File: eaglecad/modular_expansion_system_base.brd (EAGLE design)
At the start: 90.2 x 100 mm, 36 parts, among them IC1 74LS244N, IC2 74LS244N, IC3 74LS244N, IC4 SRAM, IC5 74LS30N, IC6 74LS30N, IC7 7805T, IC8 74LS00N, IC9 7805T, J1_ADDRESS_CON j1, J2_DATA_AND_POWER_CON j2, J3 interrupt_wait_block, SW1 100SP3T1B1M6QE

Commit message: all three boards designed
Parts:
- removed C9: .1uf, rcl:C025-025X050
- removed IC5: 74LS30N, 74xx-us:DIL14
- removed J3: interrupt_wait_block, SparkFun-Connectors:1X20
- removed RN1: 4.7k, resistor-dil:DIL16
- added J1-WAIT-AND-INT: WAIT-AND-INT, SparkFun-Connectors:2X4
- IC6: value 74LS30N -> 74LS20N
- RN2: device resistor-dil:DIL16 -> resistor-sil:SIL9
- moved C6 38.3 mm to (58.4, 77.5)
- moved RN2 17.2 mm to (80.6, 75.6), turned to 90 degrees
- moved IC6 7.96 mm to (69.2, 77.5), turned to 0 degrees
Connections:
- removed net INT*0: IC5.12, J3.1, RN2.8
- removed net INT*1: IC5.11, J3.2, RN2.7
- removed net INT*2: IC5.6, J3.3, RN2.6
- removed net INT*3: IC5.5, J3.4, RN2.5
- removed net INT*4: IC5.4, J3.5, RN2.4
- removed net INT*5: IC5.3, J3.6, RN2.3
- removed net INT*6: IC5.2, J3.7, RN2.2
- removed net INT*7: IC5.1, J3.8, RN2.1
- removed net N$21: IC6.3, J3.18, RN1.3
- removed net WAIT*0: IC6.12, J3.13, RN1.8
- removed net WAIT*1: IC6.11, J3.14, RN1.7
- removed net WAIT*2: IC6.6, J3.15, RN1.6
- removed net WAIT*3: IC6.5, J3.16, RN1.5
- removed net WAIT*5: IC6.4, J3.17, RN1.4
- removed net WAIT*6: IC6.2, J3.19, RN1.2
- removed net WAIT*7: IC6.1, J3.20, RN1.1
- new net INT0*: IC6.5, J1-WAIT-AND-INT.1, RN2.2
- new net INT1*: IC6.4, J1-WAIT-AND-INT.3, RN2.3
- new net INT2*: IC6.2, J1-WAIT-AND-INT.5, RN2.4
- new net INT3*: IC6.1, J1-WAIT-AND-INT.7, RN2.5
- new net WAIT0*: IC6.13, J1-WAIT-AND-INT.2, RN2.6
- new net WAIT1*: IC6.12, J1-WAIT-AND-INT.4, RN2.7
- new net WAIT2*: IC6.10, J1-WAIT-AND-INT.6, RN2.8
- new net WAIT3*: IC6.9, J1-WAIT-AND-INT.8, RN2.9
- net GND: no longer C9.2, IC5.7
- net INT: now also IC6.6; no longer IC5.8
- net VCC: now also RN2.1; no longer C9.1, IC5.14, RN1.10, RN1.11, RN1.12, RN1.13, RN1.14, RN1.15, RN1.16, RN1.9, RN2.10, RN2.11, RN2.12, RN2.13, RN2.14, RN2.15, RN2.16, RN2.9
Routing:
- net WAIT*0: track 67.5 -> 0.00 mm
- net INT2*: track 0.00 -> 58.1 mm
- net INT3*: track 0.00 -> 51.6 mm
- net WAIT*1: track 48.9 -> 0.00 mm, vias 2 -> 0
- net INT*0: track 42.1 -> 0.00 mm, vias 1 -> 0
- net INT*2: track 40.8 -> 0.00 mm
- net INT*3: track 39.5 -> 0.00 mm
- net WAIT*2: track 39.4 -> 0.00 mm
- net INT*7: track 39.0 -> 0.00 mm
- net WAIT*6: track 38.6 -> 0.00 mm
- net N$21: track 37.3 -> 0.00 mm
- net INT*4: track 36.7 -> 0.00 mm
- net WAIT*7: track 36.4 -> 0.00 mm
- net WAIT*5: track 36.3 -> 0.00 mm
- net WAIT*3: track 35.3 -> 0.00 mm
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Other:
- board text added: "INT*"
- board text added: "WAIT*"
- board text removed: "IN*0"
- board text removed: "IN*1"
- board text removed: "IN*2"
- board text removed: "IN*3"
- board text removed: "IN*4"
- board text removed: "IN*5"
- board text removed: "IN*6"
- board text removed: "IN*7"
- board text removed: "W0*"
- board text removed: "W1*"
- board text removed: "W2*"
- board text removed: "W3*"
- board text removed: "W4*"
- board text removed: "W5*"
- board text removed: "W6*"
- board text removed: "W7*"

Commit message: added text to boards
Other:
- board text added: "TRS80MXS Base - V1.0 Joe Rounceville (C) 2019"
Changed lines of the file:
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@@
 <text x="63.5" y="92.3925" size="1.778" layer="25" rot="R270">WAIT*</text>
 <text x="74.295" y="86.36" size="1.778" layer="25" rot="R90">INT*</text>
+<text x="82.55" y="31.75" size="1.778" layer="25" rot="R90">TRS80MXS Base - V1.0
+Joe Rounceville (C) 2019</text>
 </plain>
 <attributes>
@@
 </drawing>
 <compatibility>
+<note version="6.3" minversion="6.2.2" severity="warning">
+Since Version 6.2.2 text objects can contain more than one line,
+which will not be processed correctly with this version.
+</note>
 <note version="8.2" severity="warning">
 Since Version 8.2, EAGLE supports online libraries. The ids

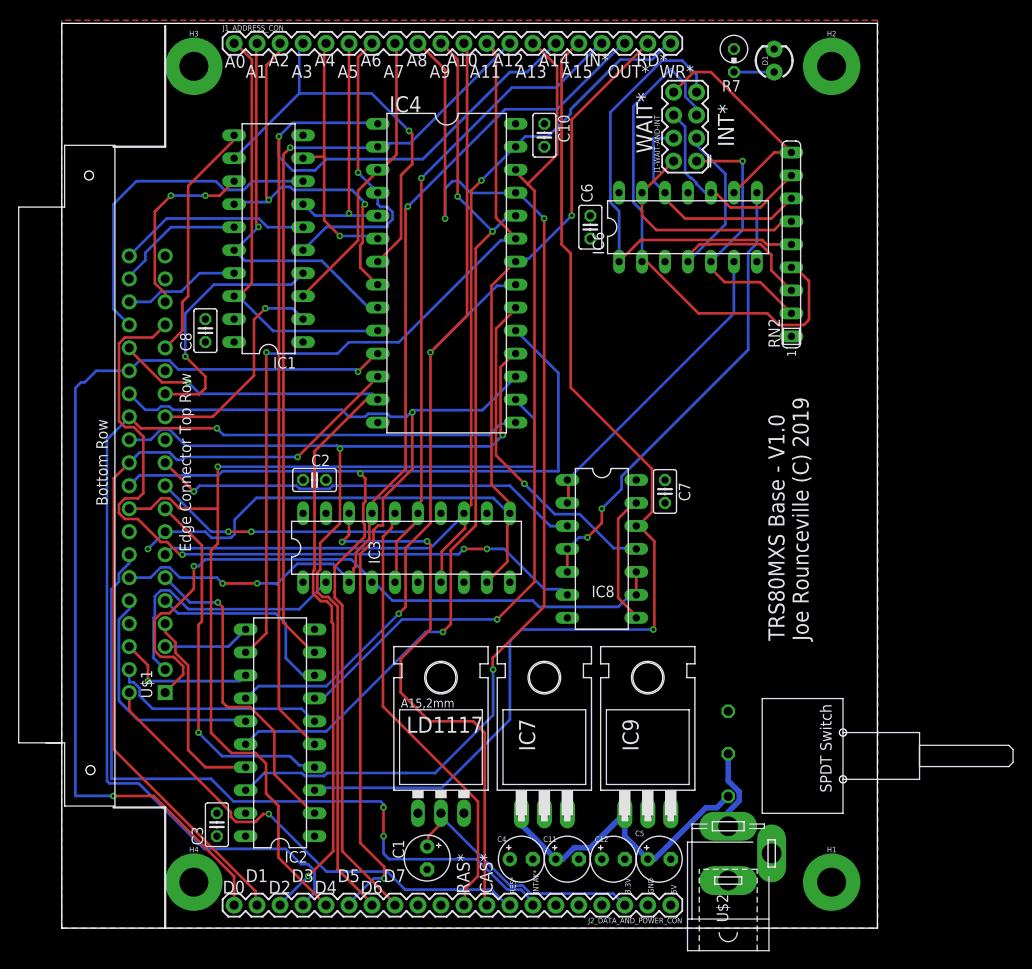
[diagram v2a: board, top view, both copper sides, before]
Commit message: removed soft reset for vdp, added 12 voice sound
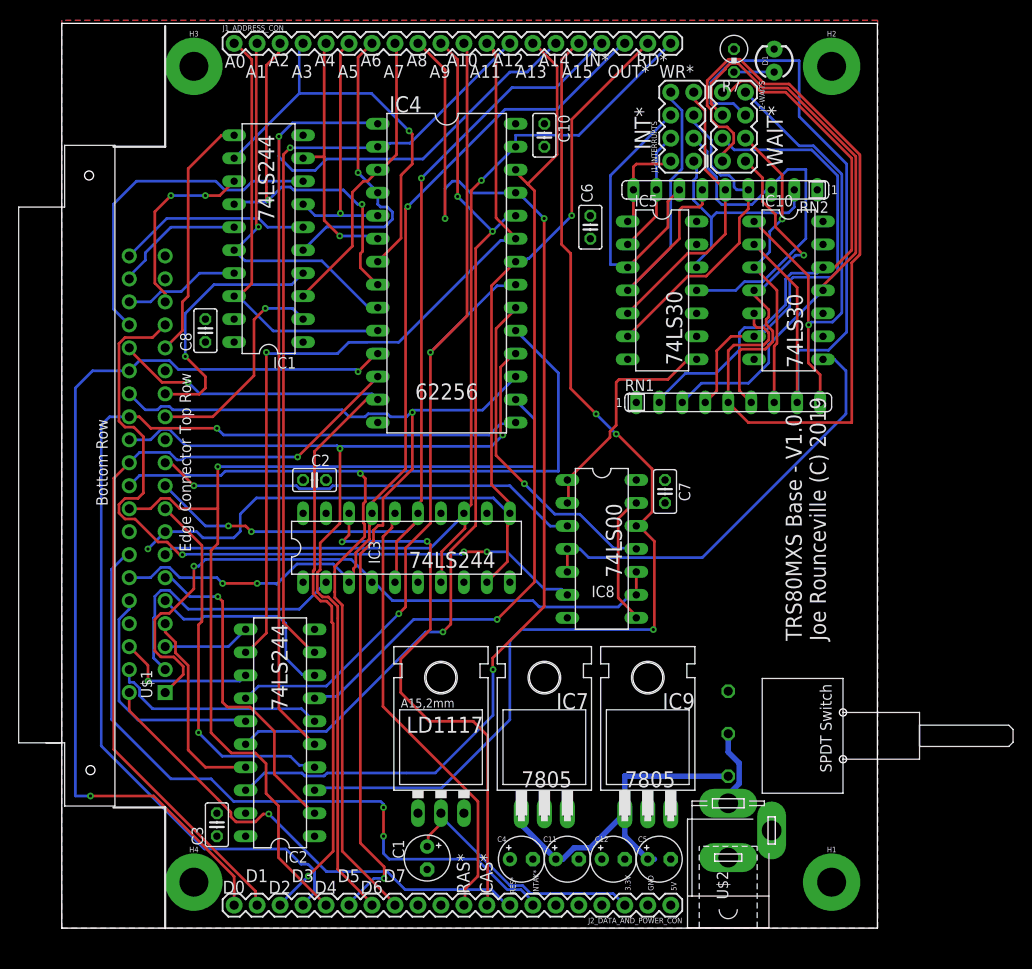
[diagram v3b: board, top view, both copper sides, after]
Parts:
- removed IC6: 74LS20N, 74xx-us:DIL14
- removed J1-WAIT-AND-INT: WAIT-AND-INT, SparkFun-Connectors:2X4
- added IC10, IC5: 74LS30N, 74xx-us:DIL14
- added J1-INTERRUPTS: INTERRUPTS, SparkFun-Connectors:2X4
- added J2-WAITS: WAITS, SparkFun-Connectors:2X4
- added RN1: 4.7k, resistor-sil:SIL9
- moved RN2 9.47 mm to (73.3, 81.6), turned to 180 degrees
- moved U$2 2.54 mm to (73.7, 10.8)
- moved SW1 2.22 mm to (73.7, 25.7)
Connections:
- new net INT4*: IC5.1, J1-INTERRUPTS.2, RN2.9
- new net INT5*: IC5.2, J1-INTERRUPTS.4, RN2.8
- new net INT6*: IC5.3, J1-INTERRUPTS.6, RN2.7
- new net INT7*: IC5.4, J1-INTERRUPTS.8, RN2.6
- new net WAIT4*: IC10.5, J2-WAITS.7, RN1.5
- new net WAIT5*: IC10.6, J2-WAITS.5, RN1.4
- new net WAIT6*: IC10.11, J2-WAITS.3, RN1.3
- new net WAIT7*: IC10.12, J2-WAITS.1, RN1.2
- net GND: now also IC10.7, IC5.7; no longer IC6.7
- net INT: now also IC5.8; no longer IC6.6
- net INT0*: now also IC5.12, J1-INTERRUPTS.1; no longer IC6.5, J1-WAIT-AND-INT.1
- net INT1*: now also IC5.11, J1-INTERRUPTS.3; no longer IC6.4, J1-WAIT-AND-INT.3
- net INT2*: now also IC5.6, J1-INTERRUPTS.5; no longer IC6.2, J1-WAIT-AND-INT.5
- net INT3*: now also IC5.5, J1-INTERRUPTS.7; no longer IC6.1, J1-WAIT-AND-INT.7
- net VCC: now also IC10.14, IC5.14, RN1.1; no longer IC6.14
- net WAIT: now also IC10.8; no longer IC6.8
- net WAIT0*: now also IC10.4, J2-WAITS.8, RN1.6; no longer IC6.13, J1-WAIT-AND-INT.2, RN2.6
- net WAIT1*: now also IC10.3, J2-WAITS.6, RN1.7; no longer IC6.12, J1-WAIT-AND-INT.4, RN2.7
- net WAIT2*: now also IC10.2, J2-WAITS.4, RN1.8; no longer IC6.10, J1-WAIT-AND-INT.6, RN2.8
- net WAIT3*: now also IC10.1, J2-WAITS.2, RN1.9; no longer IC6.9, J1-WAIT-AND-INT.8, RN2.9
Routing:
- net WAIT4*: track 0.00 -> 92.7 mm
- net WAIT6*: track 0.00 -> 63.4 mm
- net WAIT7*: track 0.00 -> 59.7 mm
- net WAIT2*: track 21.8 -> 81.1 mm
- net WAIT5*: track 0.00 -> 49.9 mm
- net INT7*: track 0.00 -> 40.6 mm
- net INT6*: track 0.00 -> 32.2 mm
- net WAIT3*: track 25.8 -> 57.0 mm, vias 0 -> 1
- net INT2*: track 58.1 -> 34.9 mm
- net INT3*: track 51.6 -> 31.6 mm
- net INT5*: track 0.00 -> 13.7 mm
- net WAIT0*: track 25.0 -> 37.3 mm, vias 0 -> 1
- net INT4*: track 0.00 -> 10.7 mm
- net INT1*: track 32.4 -> 41.9 mm
- net INT: track 34.6 -> 25.7 mm
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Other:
- board text added: "62256"
- board text added: "74LS00"
- board text added: "74LS244"
- board text added: "74LS30"
- board text added: "7805"

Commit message: boards as they were when sent to allpcb
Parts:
- moved R7 3.86 mm to (70.5, 96.5), turned to 90 degrees
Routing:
- net N$20: track 4.45 -> 9.57 mm
- net BUFFERED_CAS*: track 61.5 -> 58.7 mm
- net BUFFERED_RD*: track 114.0 -> 111.3 mm, vias 2 -> 1
- net RAS*: track 74.0 -> 71.9 mm
- net WAIT4*: track 92.7 -> 90.8 mm
- net WAIT6*: track 63.4 -> 61.9 mm
- net BUFFERED_A13: track 94.2 -> 93.1 mm
- net VOLTAGE-IN: track 38.8 -> 38.1 mm
- net A5: track 20.6 -> 21.3 mm
- net D5: track 106.9 -> 107.6 mm
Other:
- board text added: "100uf"
- board text added: "10uf"
- board text added: "4.7k"

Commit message: bug in the base board RD, WR, IN, and OUT signals
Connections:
- new net IN*: IC3.15, U$1.P$19
- new net OUT*: IC3.17, U$1.P$12
- new net RD*: IC3.11, U$1.P$15
- new net WR*: IC3.13, U$1.P$13
- net BUFFERED_IN*: no longer IC3.15, U$1.P$19
- net BUFFERED_OUT*: no longer IC3.17, U$1.P$12
- net BUFFERED_RD*: no longer IC3.11, U$1.P$15
- net BUFFERED_WR*: no longer IC3.13, U$1.P$13
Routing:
- net BUFFERED_RD*: track 111.3 -> 0.00 mm, vias 1 -> 0
- net BUFFERED_WR*: track 109.4 -> 0.00 mm, vias 1 -> 0
- net BUFFERED_IN*: track 103.4 -> 0.00 mm, vias 3 -> 0
- net BUFFERED_OUT*: track 103.3 -> 0.00 mm, vias 3 -> 0
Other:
- board text added: "TRS80MXS Base - V1.1 Joe Rounceville (C) 2019"
- board text removed: "TRS80MXS Base - V1.0 Joe Rounceville (C) 2019"

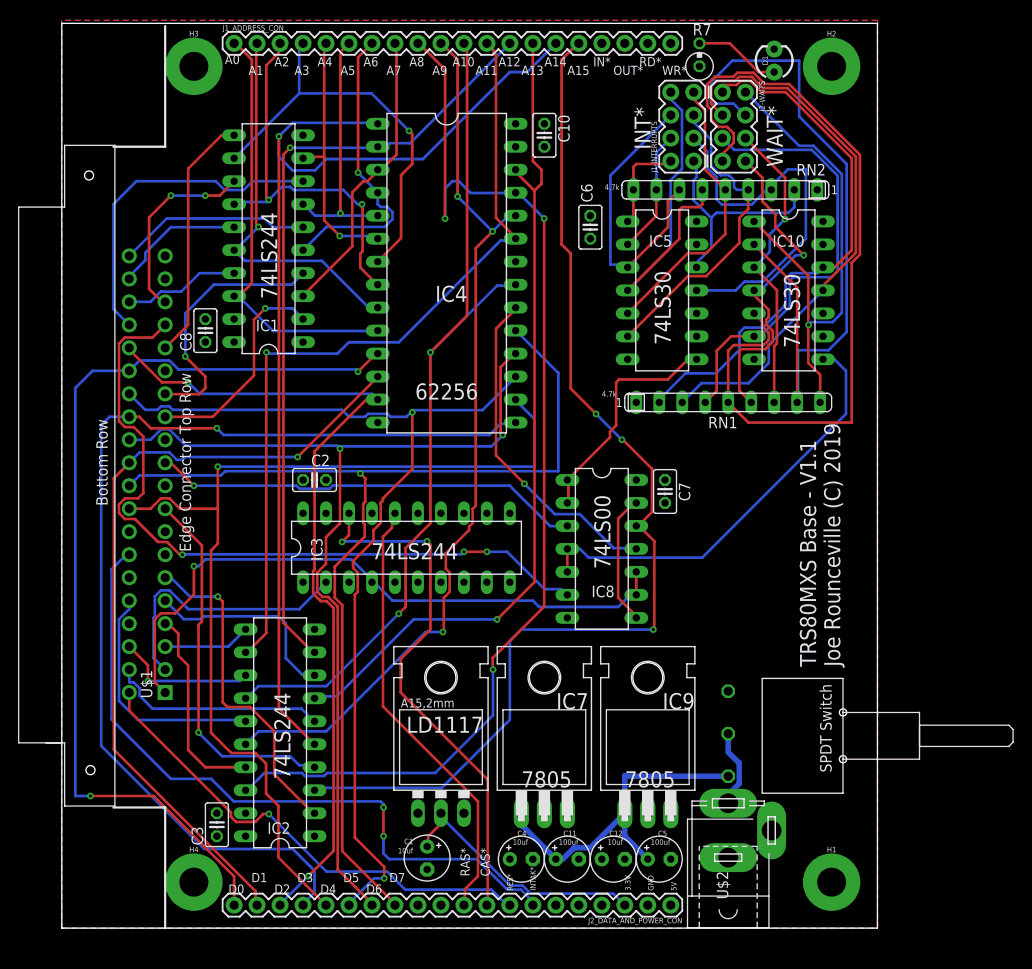
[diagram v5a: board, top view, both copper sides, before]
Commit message: fix for screwed up base board signals
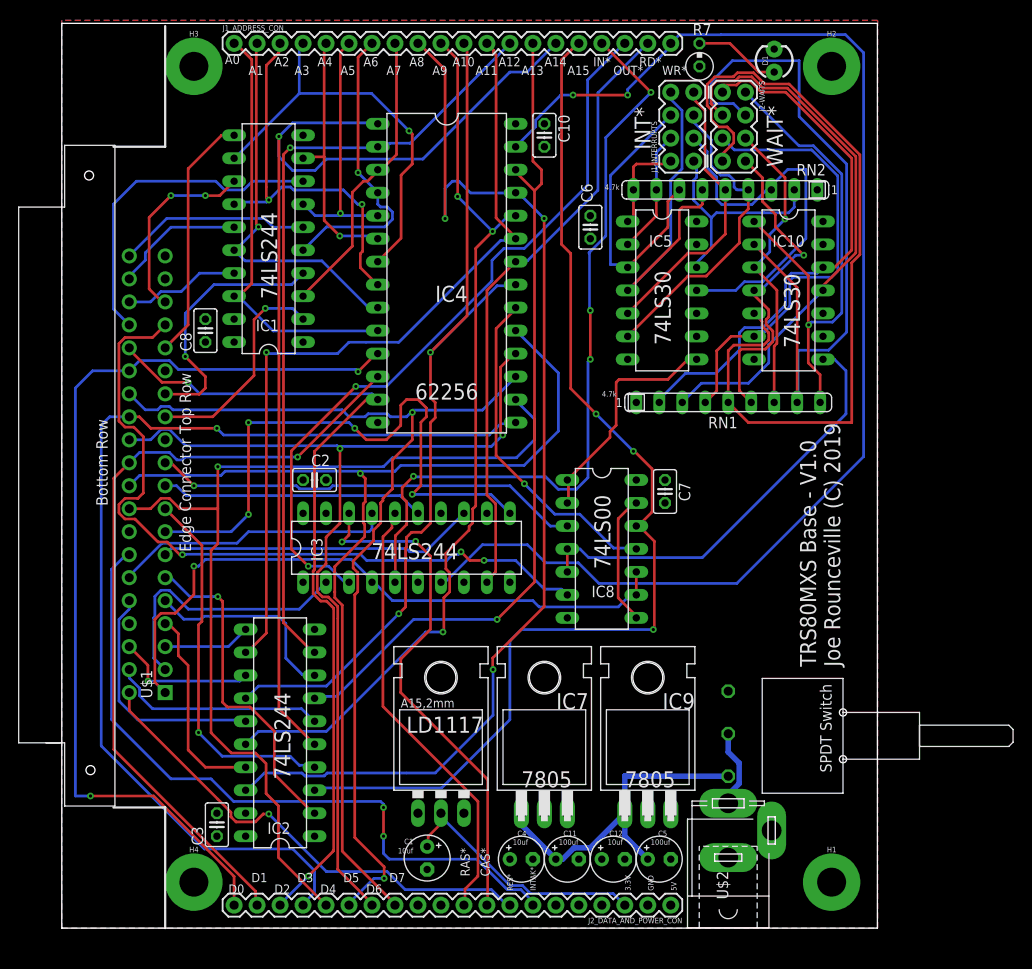
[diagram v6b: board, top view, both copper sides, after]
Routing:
- net BUFFERED_WR*: track 0.00 -> 146.1 mm, vias 0 -> 2
- net BUFFERED_IN*: track 0.00 -> 86.7 mm, vias 0 -> 4
- net BUFFERED_OUT*: track 0.00 -> 82.4 mm, vias 0 -> 2
- net BUFFERED_RD*: track 0.00 -> 68.5 mm
- net RD*: track 0.00 -> 66.0 mm, vias 0 -> 4
- net WR*: track 0.00 -> 35.2 mm
- net OUT*: track 0.00 -> 30.9 mm
- net IN*: track 0.00 -> 29.2 mm
- net D7: track 118.0 -> 115.5 mm
- net D4: track 109.6 -> 107.9 mm
- net BUFFERED_A10: track 99.6 -> 100.7 mm
- net BUFFERED_CAS*: track 58.7 -> 57.9 mm
- net WAIT*: track 81.9 -> 82.5 mm
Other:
- board text added: "TRS80MXS Base - V1.0 Joe Rounceville (C) 2019"
- board text removed: "TRS80MXS Base - V1.1 Joe Rounceville (C) 2019"
